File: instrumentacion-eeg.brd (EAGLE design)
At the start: 63.4 x 80 mm, 39 parts, among them IC1 LMV321AIDCKR, IC15 LMV321AIDCKR, IC16 LMV321AIDCKR, IC2 ESP32-S3-WROOM-1-N4R2, IC3 LMV321AIDCKR, IC5 MCP73831T-2ACI_OT, IC7 AD8226ARZ, IC9 LP38692MP-3.3_NOPB, J1 USB3500-30-A-KIT, J3 SJ-3523-SMT-TR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

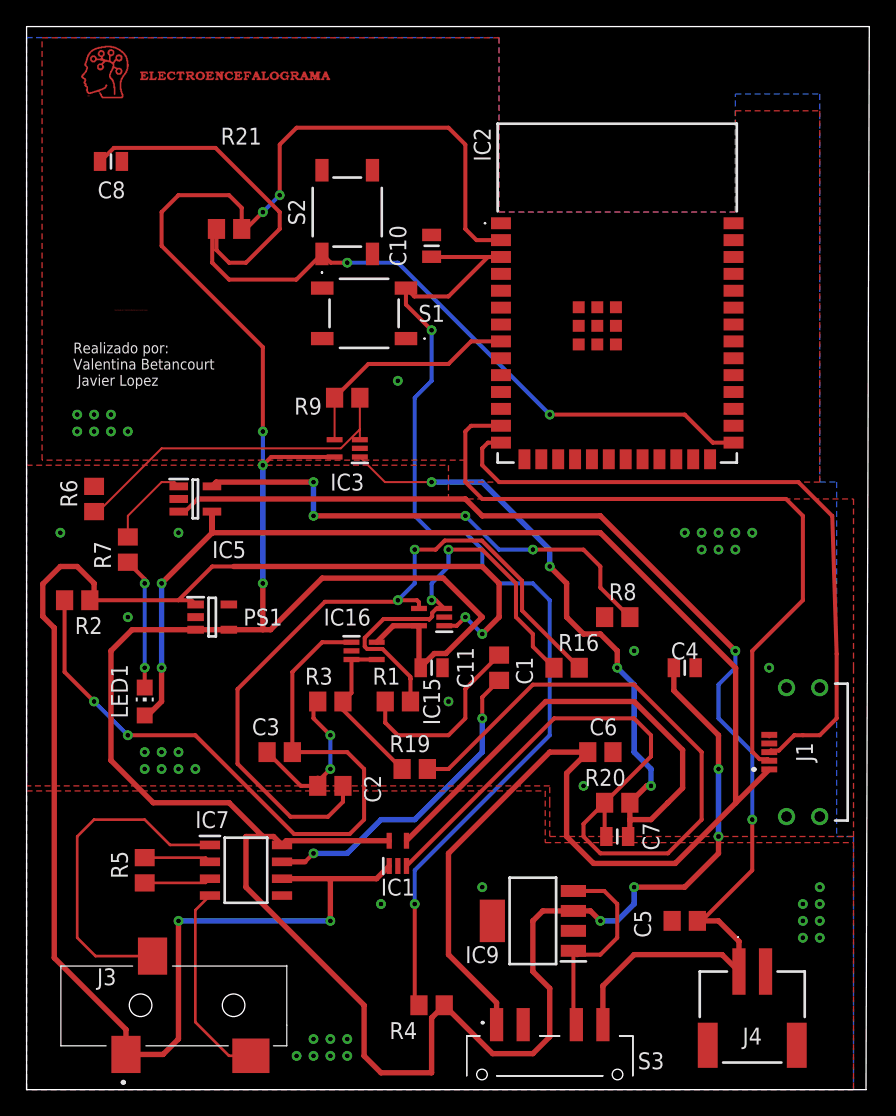
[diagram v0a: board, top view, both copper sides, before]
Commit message: fix: algunos errores corregidos en el PCB
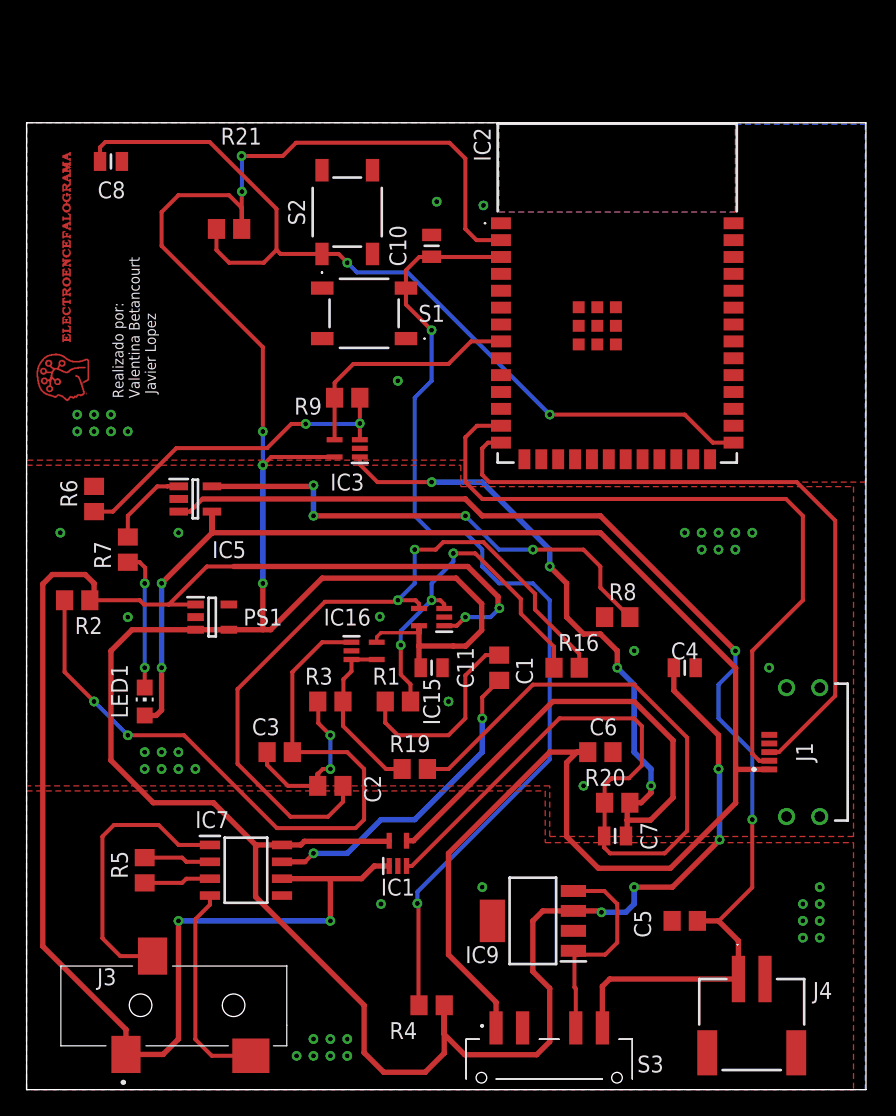
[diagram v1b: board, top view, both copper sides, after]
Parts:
- moved J4 0.57 mm to (54.6, 8.32)
- moved S3 0.25 mm to (39.3, 2.30)
- moved C7 0.17 mm to (44.3, 19.1)
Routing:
- net N$13: track 74.4 -> 67.4 mm
- net N$46: track 33.2 -> 27.2 mm, vias 2 -> 3
- net N$9: track 76.8 -> 71.6 mm
- net N$11: track 25.2 -> 21.1 mm
- net +3V3: track 245.0 -> 242.9 mm
- net VSS: track 122.7 -> 121.0 mm
- net +BATT: track 91.2 -> 90.2 mm
- net N$4: track 12.8 -> 13.6 mm
- net N$1: track 15.2 -> 16.0 mm
- net N$6: track 12.2 -> 13.0 mm
- net OUT-EEG: track 17.4 -> 18.1 mm
- net +D: track 52.1 -> 51.5 mm
- net N$2: track 14.4 -> 14.9 mm
- net N$20: track 9.96 -> 10.5 mm
- net N$14: track 25.7 -> 26.0 mm, vias 0 -> 2
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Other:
- board size 63.4 x 80 mm -> 63.2 x 72.8 mm
- board text removed: "Realizado por: Valentina Betancourt, Javier Lopez"
